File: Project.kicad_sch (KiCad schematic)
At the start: 12 parts, among them U1 AMS1117-3.3, U2 ESP32-WROOM-32

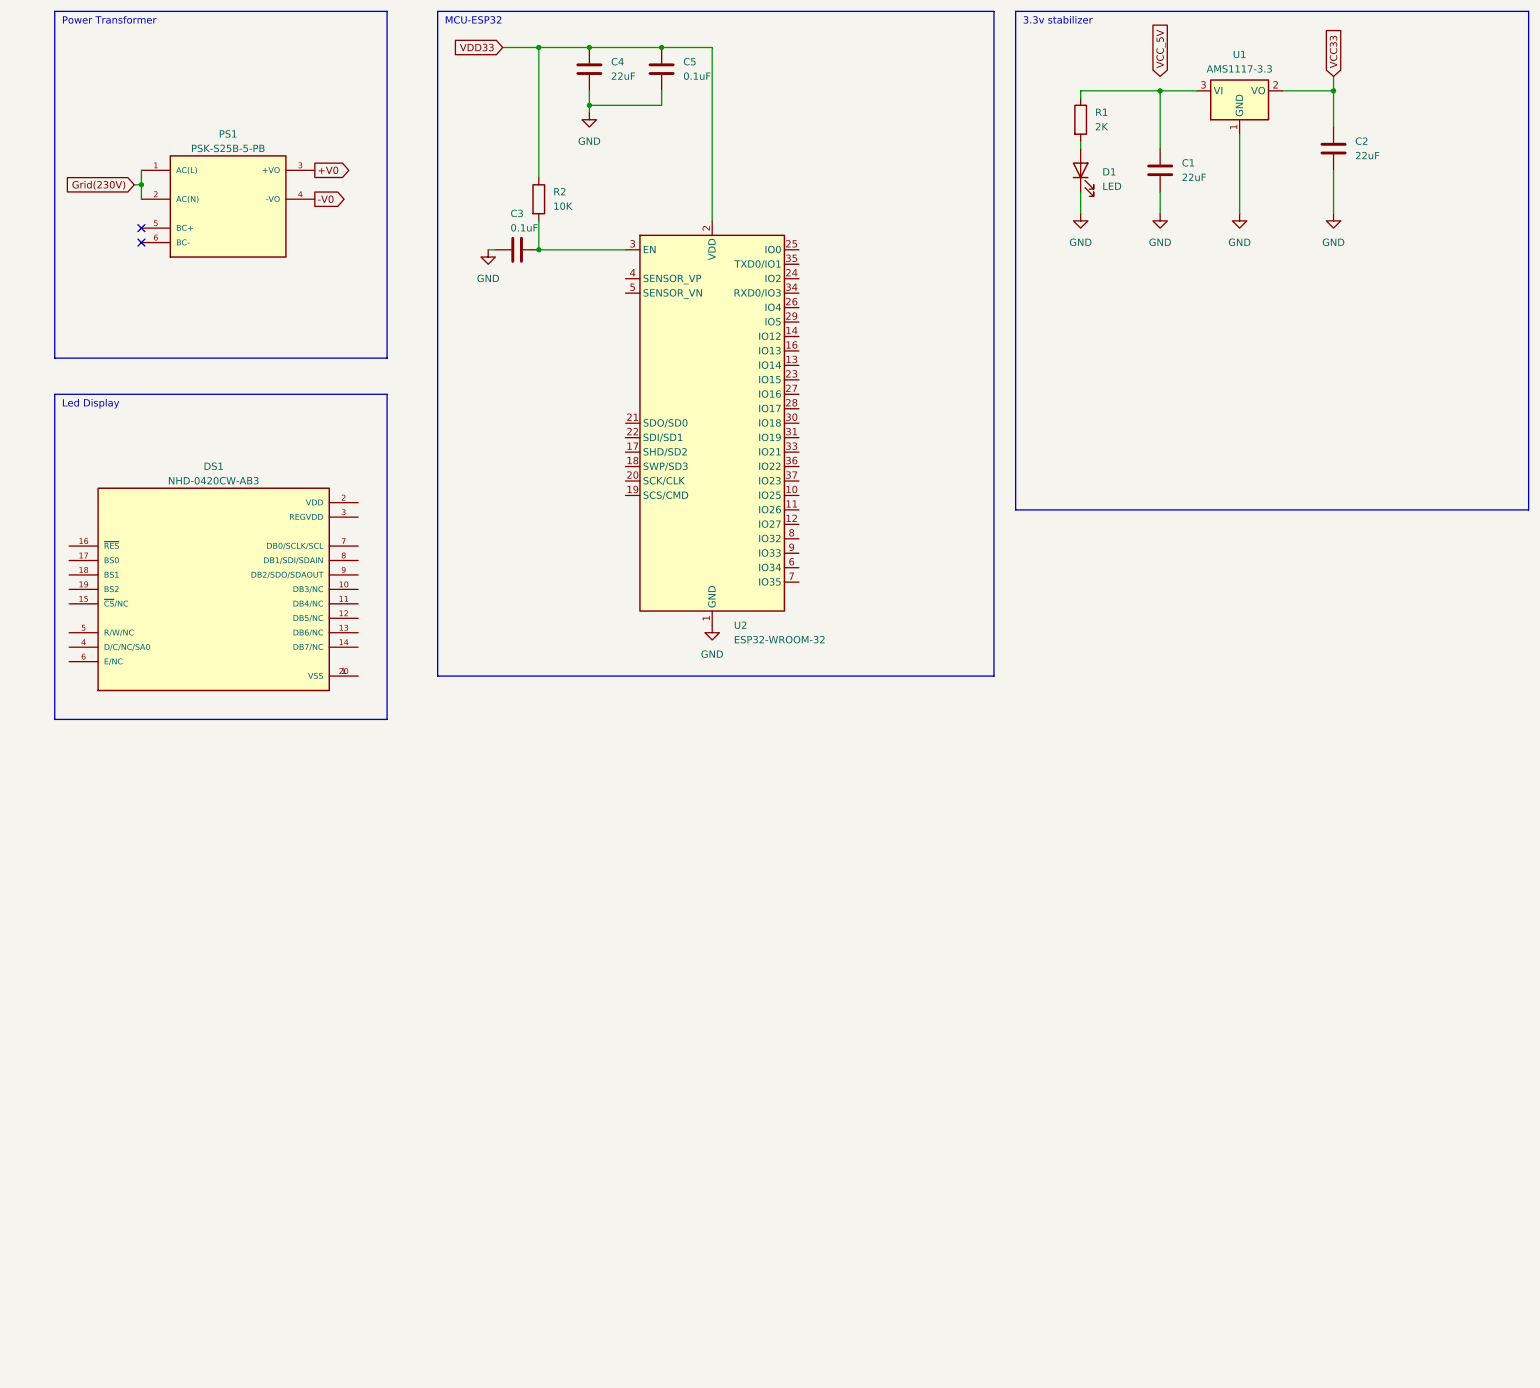
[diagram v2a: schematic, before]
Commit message: AC dimmer
Added AC dimmer and conectors
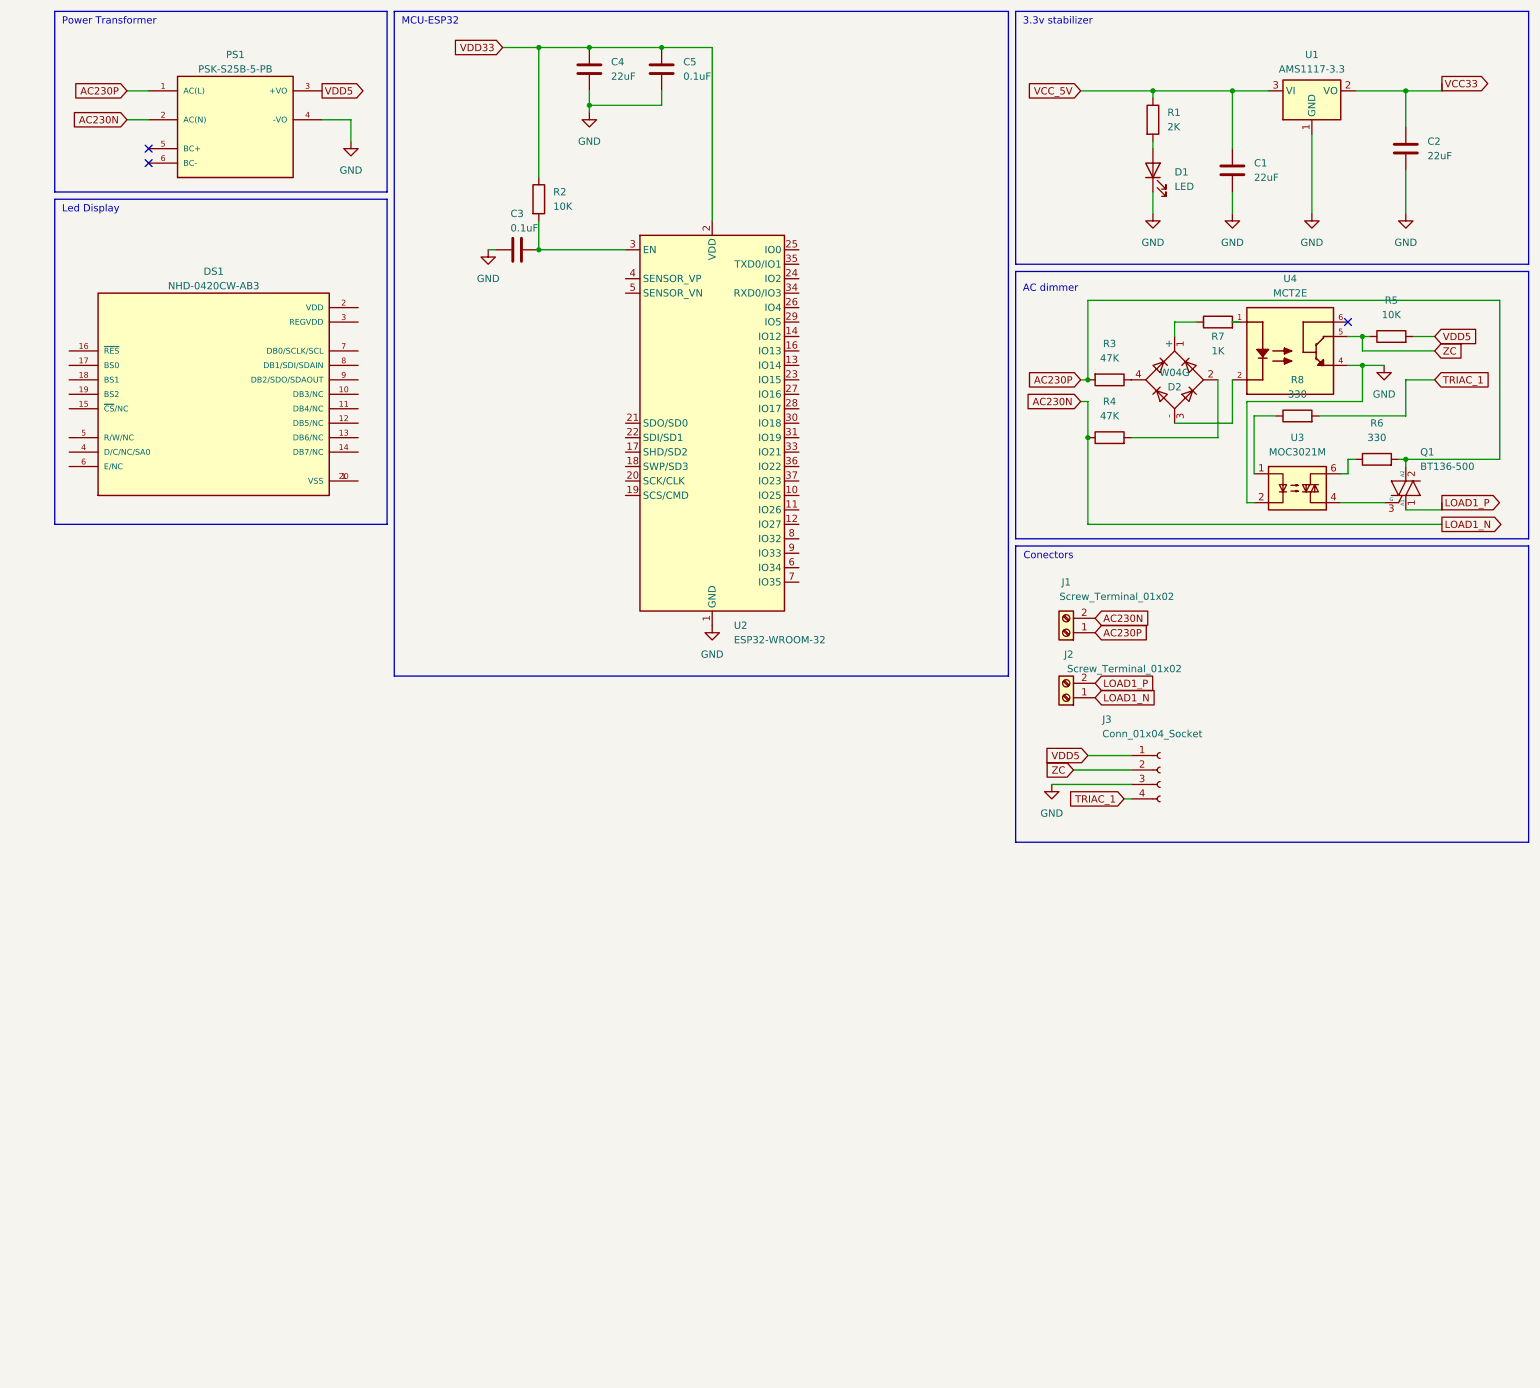
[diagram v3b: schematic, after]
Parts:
- added D2: W04G, Diode_THT:Diode_Bridge_Round_D9.8mm, symbol Diode_Bridge:W04G
- added J1, J2: Screw_Terminal_01x02, TerminalBlock_RND:TerminalBlock_RND_205-00012_1x02_P5.00mm_Horizontal, symbol Connector:Screw_Terminal_01x02
- added J3: Conn_01x04_Socket, Connector_PinHeader_1.27mm:PinHeader_1x04_P1.27mm_Vertical, symbol Connector:Conn_01x04_Socket
- added Q1: BT136-500, Package_TO_SOT_THT:TO-220-3_Vertical, symbol Triac_Thyristor:BT136-500
- added R3, R4: 47K, symbol Device:R
- added R5: 10K, symbol Device:R
- added R6, R8: 330, symbol Device:R
- added R7: 1K, symbol Device:R
- added U3: MOC3021M, symbol Relay_SolidState:MOC3021M
- added U4: MCT2E, MCT2E:DIP762W50P254L742H480Q6, symbol MCT2E:MCT2E
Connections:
- net -V0 is gone; now on net GND: PS1.4 (-VO)
- net GND: now also J3.3 (Pin_3), U3.2, U4.4
- net VCC_5V: now also C1.1, R1.1, U1.3 (VI)
- net +V0 renamed VDD5
- net VDD5: now also J3.1 (Pin_1), R5.2
- net Grid(230V) renamed AC230N
- net AC230N: now also J1.2 (Pin_2), J2.1 (Pin_1), R4.1; no longer PS1.1 (AC(L))
- new net: D2.2, R4.2
- new net: D2.1 (+), R7.1
- new net: D2.3 (-), U4.2
- new net: D2.4, R3.1
- new net: R6.1, U3.6
- new net: R7.2, U4.1
- new net: R8.1, U3.1
- new net: Q1.3 (G), U3.4
- new net AC230P: J1.1 (Pin_1), PS1.1 (AC(L)), Q1.2 (A2), R3.2, R6.2
- new net LOAD1_P: J2.2 (Pin_2), Q1.1 (A1)
- new net TRIAC_1: J3.4 (Pin_4), R8.2
- new net ZC: J3.2 (Pin_2), R5.1, U4.5
- no-connect marks 2 -> 3
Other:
- note added: "AC dimmer"
- note added: "Conectors"
- title: (none) -> Home Light System
- moved on the sheet: C1, C2, D1, DS1, PS1, R1, U1

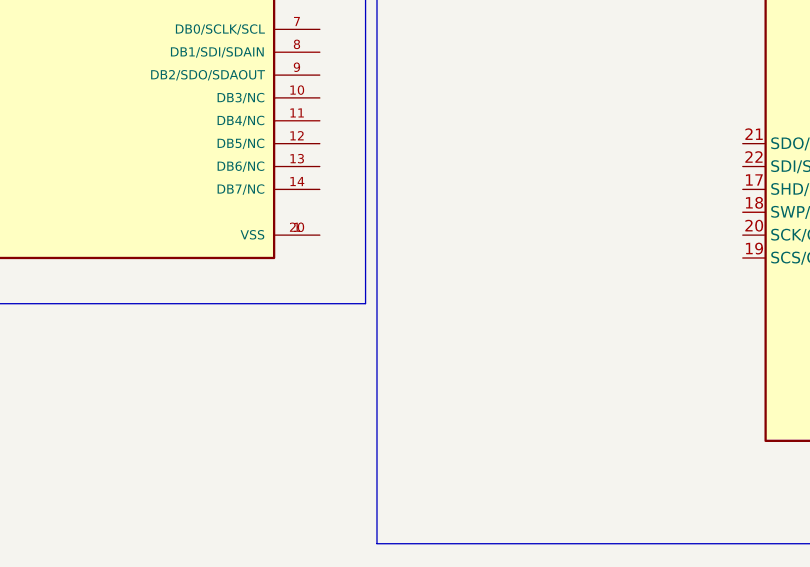
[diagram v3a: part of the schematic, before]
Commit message: Footprints, prices
All available components got assigned with their footprints, price-list is updated
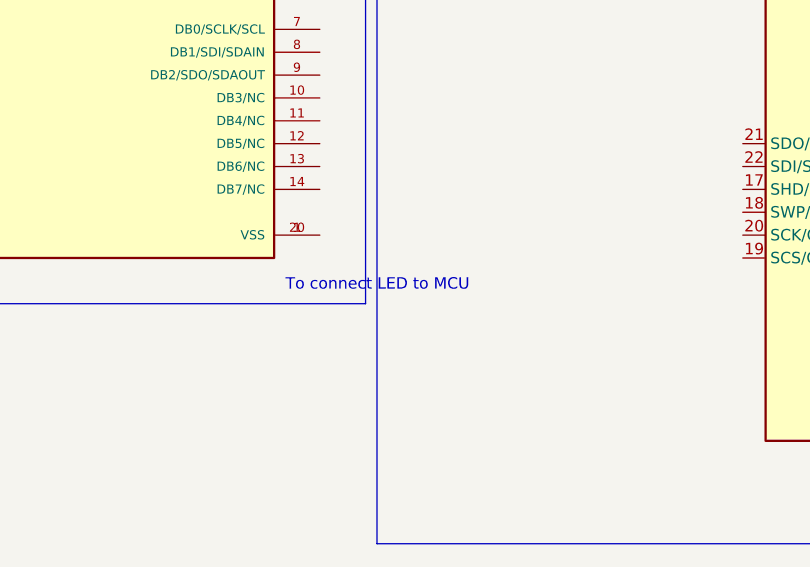
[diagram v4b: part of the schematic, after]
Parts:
- C1, C2, C4: footprint (none) -> Capacitor_22uF:PCAP_125x25_PAN
- C3, C5: footprint (none) -> Capacitor_0_1uF:CAP_BFC233814104_VIS
- D1: footprint (none) -> Red_LED:LED_SSL-LX30_T-3_LUM
- R1: footprint (none) -> Resistor_2k:RES_TYCO_YR1_TYC
- R2, R5: footprint (none) -> Resistor_10k:RES_CFR25_TYCO_TYC
- R3, R4: footprint (none) -> Resistor_47k:RES_CFR50_TYCO_TYC
- R6, R8: footprint (none) -> Resistor_330:RES_LR1_TYCO_TYC
- R7: footprint (none) -> Resistor_1k:RES_CFR200_TYCO_TYC
- U3: footprint (none) -> Triac_BTA16:TO-220AB_STM
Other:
- note added: "To connect LED to MCU"
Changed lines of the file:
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@@
+    (effects (font (size 1.27 1.27)) (justify left bottom))
+  )
+  (text "To connect LED to MCU" (at 71.12 107.95 0)
     (effects (font (size 1.27 1.27)) (justify left bottom))
   )
@@
       (effects (font (size 1.27 1.27)))
     )
-    (property "Footprint" "" (at 207.01 95.758 90)
+    (property "Footprint" "Resistor_47k:RES_CFR50_TYCO_TYC" (at 207.01 95.758 90)
       (effects (font (size 1.27 1.27)) hide)
     )
@@
       (effects (font (size 1.27 1.27)) (justify left))
     )
-    (property "Footprint" "" (at 212.852 38.1 90)
+    (property "Footprint" "Resistor_2k:RES_TYCO_YR1_TYC" (at 212.852 38.1 90)
       (effects (font (size 1.27 1.27)) hide)
     )
@@
       (effects (font (size 1.27 1.27)))
     )
-    (property "Footprint" "" (at 256.54 77.978 90)
+    (property "Footprint" "Resistor_10k:RES_CFR25_TYCO_TYC" (at 256.54 77.978 90)
       (effects (font (size 1.27 1.27)) hide)
     )
@@
       (effects (font (size 1.27 1.27)) (justify left))
     )
-    (property "Footprint" "" (at 129.2352 33.02 0)
+    (property "Footprint" "Capacitor_0_1uF:CAP_BFC233814104_VIS" (at 129.2352 33.02 0)
       (effects (font (size 1.27 1.27)) hide)
     )
@@
       (effects (font (size 1.27 1.27)))
     )
-    (property "Footprint" "" (at 254 99.568 90)
+    (property "Footprint" "Resistor_330:RES_LR1_TYCO_TYC" (at 254 99.568 90)
       (effects (font (size 1.27 1.27)) hide)
     )
@@
       (effects (font (size 1.27 1.27)) (justify left))
     )
-    (property "Footprint" "" (at 229.5652 50.8 0)
+    (property "Footprint" "Capacitor_22uF:PCAP_125x25_PAN" (at 229.5652 50.8 0)
       (effects (font (size 1.27 1.27)) hide)
     )
@@
       (effects (font (size 1.27 1.27)) (justify right))
     )
-    (property "Footprint" "" (at 214.63 46.99 0)
+    (property "Footprint" "Red_LED:LED_SSL-LX30_T-3_LUM" (at 214.63 46.99 0)
       (effects (font (size 1.27 1.27)) hide)
     )
@@
       (effects (font (size 1.27 1.27)))
     )
-    (property "Footprint" "" (at 240.03 91.948 90)
+    (property "Footprint" "Resistor_330:RES_LR1_TYCO_TYC" (at 240.03 91.948 90)
       (effects (font (size 1.27 1.27)) hide)
     )
@@
       (effects (font (size 1.27 1.27)) (justify left))
     )
-    (property "Footprint" "" (at 104.902 52.07 90)
+    (property "Footprint" "Resistor_10k:RES_CFR25_TYCO_TYC" (at 104.902 52.07 90)
       (effects (font (size 1.27 1.27)) hide)
     )
@@
       (effects (font (size 1.27 1.27)))
     )
-    (property "Footprint" "" (at 207.01 82.042 90)
+    (property "Footprint" "Resistor_47k:RES_CFR50_TYCO_TYC" (at 207.01 82.042 90)
       (effects (font (size 1.27 1.27)) hide)
     )
@@
       (effects (font (size 1.27 1.27)))
     )
-    (property "Footprint" "" (at 226.06 75.438 90)
+    (property "Footprint" "Resistor_1k:RES_CFR200_TYCO_TYC" (at 226.06 75.438 90)
       (effects (font (size 1.27 1.27)) hide)
     )
@@
       (effects (font (size 1.27 1.27)))
     )
-    (property "Footprint" "" (at 106.68 59.9948 0)
+    (property "Footprint" "Capacitor_0_1uF:CAP_BFC233814104_VIS" (at 106.68 59.9948 0)
       (effects (font (size 1.27 1.27)) hide)
     )
@@
       (effects (font (size 1.27 1.27)) (justify left))
     )
-    (property "Footprint" "" (at 260.0452 46.99 0)
+    (property "Footprint" "Capacitor_22uF:PCAP_125x25_PAN" (at 260.0452 46.99 0)
       (effects (font (size 1.27 1.27)) hide)
     )
@@
       (effects (font (size 1.27 1.27)) (justify left))
     )
-    (property "Footprint" "" (at 116.5352 33.02 0)
+    (property "Footprint" "Capacitor_22uF:PCAP_125x25_PAN" (at 116.5352 33.02 0)
       (effects (font (size 1.27 1.27)) hide)
     )
@@
       (effects (font (size 1.27 1.27)))
     )
-    (property "Footprint" "" (at 234.95 107.95 0)
+    (property "Footprint" "Triac_BTA16:TO-220AB_STM" (at 234.95 107.95 0)
       (effects (font (size 1.27 1.27) italic) (justify left) hide)
     )

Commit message: Added 3d models
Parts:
- U3: footprint Triac_BTA16:TO-220AB_STM -> MOC3021M:PDIP6_BX_ONS
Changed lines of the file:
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@@
       (effects (font (size 1.27 1.27)))
     )
-    (property "Footprint" "Triac_BTA16:TO-220AB_STM" (at 234.95 107.95 0)
+    (property "Footprint" "MOC3021M:PDIP6_BX_ONS" (at 234.95 107.95 0)
       (effects (font (size 1.27 1.27) italic) (justify left) hide)
     )
